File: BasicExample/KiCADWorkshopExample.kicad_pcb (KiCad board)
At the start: 2 copper layers, 100 x 100 mm, 21 parts, among them P1 USB_C_Plug_USB2.0, SW1 SW_Push, SW2 SW_Push, SW3 SW_Push, SW4 SW_Push, U1 BD30FC0WFP

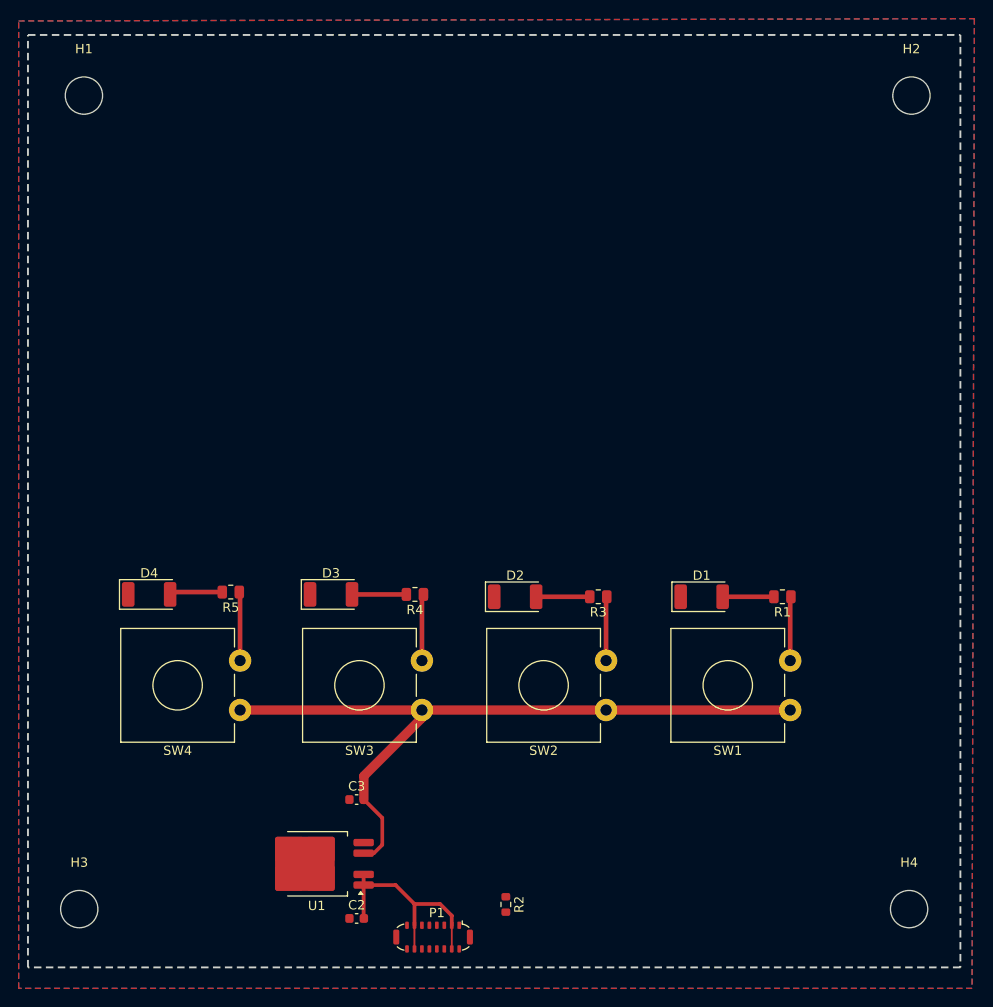
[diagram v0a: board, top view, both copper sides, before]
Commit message: complete simple tut
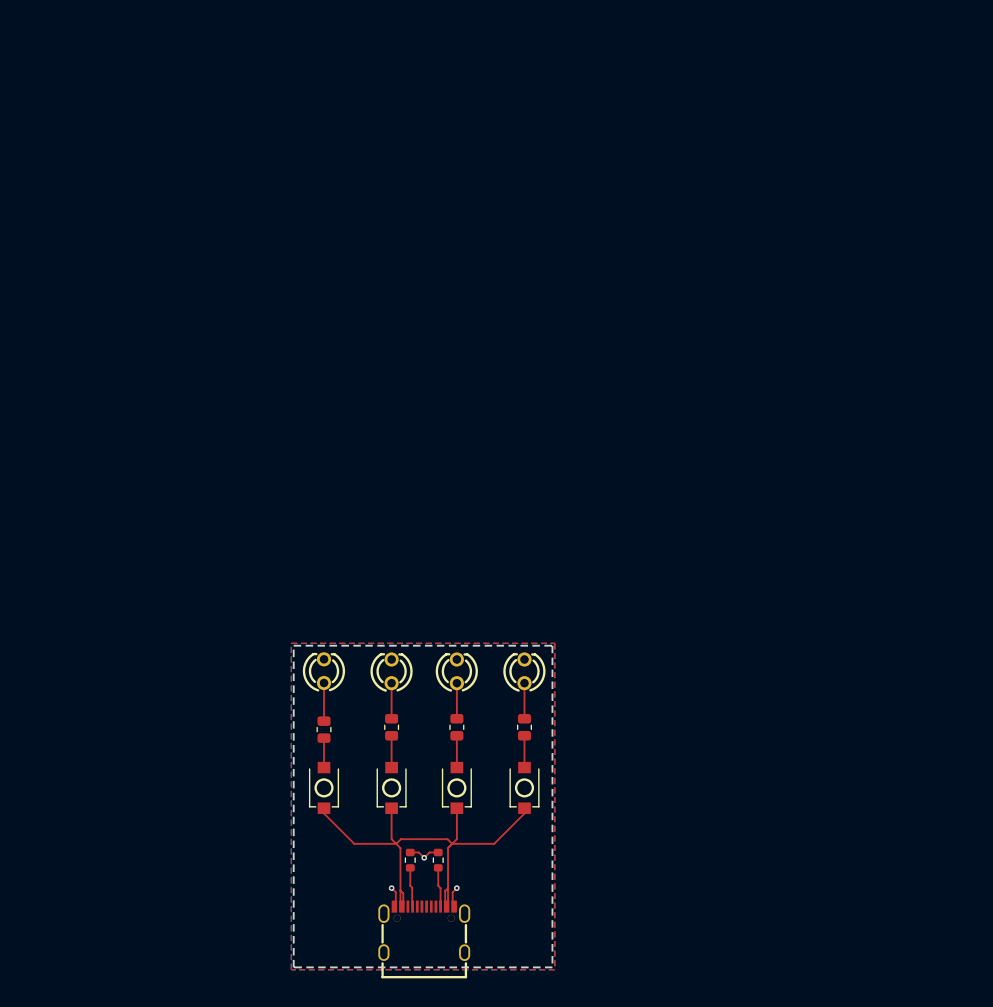
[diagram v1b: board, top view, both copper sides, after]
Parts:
- removed C2, C3: 10uF, Capacitor_SMD:C_0603_1608Metric
- removed D1, D2, D3, D4: LED, LED_SMD:LED_2010_5025Metric
- removed H1, H2, H3, H4: MountingHole, MountingHole:MountingHole_4mm
- removed P1: USB_C_Plug_USB2.0, Connector_USB:USB_C_Plug_ShenzhenJingTuoJin_918-118A2021Y40002_Vertical
- removed U1: BD30FC0WFP, Package_TO_SOT_SMD:TO-252-4
- added LED1: 204-10SURD/S530-A3-L, red:LED-TH_BD3.0-P2.54-FD, F.Cu at (103.2, 118.2)
- added LED2: 204-10SURD/S530-A3-L, red:LED-TH_BD3.0-P2.54-FD, F.Cu at (96.0, 118.2)
- added LED3: 204-10SURD/S530-A3-L, red:LED-TH_BD3.0-P2.54-FD, F.Cu at (89.0, 118.2)
- added LED4: 204-10SURD/S530-A3-L, red:LED-TH_BD3.0-P2.54-FD, F.Cu at (81.8, 118.2)
- added R6: 5K1, Resistor_SMD:R_0603_1608Metric, F.Cu at (94.0, 138.5)
- added USBC1: TYPE-C-31-M-12, usbc:USB-C_SMD-TYPE-C-31-M-12, F.Cu at (92.5, 145.9)
- R1, R3, R4, R5: value 520 -> 250
- SW1, SW2, SW3, SW4: value SW_Push -> TS-1088-AR02016; footprint Button_Switch_THT:SW_CW_GPTS203211B -> ts-1088:SW-SMD_L3.9-W3.0-P4.45
- moved R1 31.0 mm to (103.2, 124.2), turned to 90 degrees
- moved SW1 29.7 mm to (103.2, 130.8), turned to 90 degrees
- moved R3 20.6 mm to (96.0, 124.2), turned to 90 degrees
- moved SW2 18.0 mm to (96.0, 130.8), turned to 90 degrees
- moved R5 17.8 mm to (81.8, 124.5), turned to 90 degrees
- moved R4 14.5 mm to (89.0, 124.2), turned to 90 degrees
- moved SW4 12.3 mm to (81.8, 130.8), turned to 90 degrees
- moved R2 11.3 mm to (91.0, 138.5), turned to 90 degrees
- moved SW3 8.96 mm to (89.0, 130.8), turned to 90 degrees
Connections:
- SW1 pad 1: +3V3 -> VBUS
- SW2 pad 1: +3V3 -> VBUS
- SW3 pad 1: +3V3 -> VBUS
- SW4 pad 1: +3V3 -> VBUS
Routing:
- net +3V3: track 79.6 -> 0.00 mm
- net VBUS: track 23.9 -> 52.2 mm
- net GND: track 0.00 -> 7.80 mm, vias 0 -> 3
- net Net-(USBC1-CC1): track 0.00 -> 4.27 mm
- net Net-(USBC1-CC2): track 0.00 -> 4.26 mm
- net Net-(R5-Pad1): track 7.39 -> 3.16 mm
- net Net-(R4-Pad1): track 7.17 -> 3.41 mm
- net Net-(R3-Pad1): track 6.88 -> 3.41 mm
- net Net-(R1-Pad1): track 6.88 -> 3.41 mm
- net Net-(LED3-A): track 5.84 -> 3.82 mm
- net Net-(LED2-A): track 5.75 -> 3.82 mm
- net Net-(LED1-A): track 5.50 -> 3.82 mm
- net Net-(LED4-A): track 5.69 -> 4.09 mm
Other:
- board size 100 x 100 mm -> 27.8 x 34.5 mm

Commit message: traces
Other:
- board text added: "JAS"
- board text added: "JAS KiCAD Wrkshp 2024"
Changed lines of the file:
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@@
 		(layer "Edge.Cuts")
+	)
+	(gr_text "JAS KiCAD Wrkshp 2024"
+		(at 101.25 140.5 0)
+		(layer "B.SilkS")
+		(effects
+			(font
+				(size 1 1)
+				(thickness 0.2)
+				(bold yes)
+			)
+			(justify left bottom mirror)
+		)
+	)
+	(gr_text "JAS"
+		(at 101.75 149.25 0)
+		(layer "F.SilkS")
+		(effects
+			(font
+				(face "Lato")
+				(size 1.5 1.5)
+				(thickness 0.3)
+				(bold yes)
+			)
+			(justify left bottom)
+		)
+		(render_cache "JAS" 0
+			(polygon
+				(pts
+					(xy 102.525593 148.461573) (xy 102.52248 148.538488) (xy 102.511866 148.617227) (xy 102.493719 148.689818)
+					(xy 102.465709 148.761379) (xy 102.425482 148.829253) (xy 102.399563 148.861643) (xy 102.344183 148.913354)
+					(xy 102.279248 148.954181) (xy 102.246057 148.969354) (xy 102.174255 148.992126) (xy 102.095138 149.004388)
+					(xy 102.038328 149.006723) (xy 101.964718 149.003043) (xy 101.886951 148.992004) (xy 101.812648 148.975582)
+					(xy 101.81851 148.907072) (xy 101.824738 148.849187) (xy 101.841957 148.814382) (xy 101.88299 148.80046)
+					(xy 101.93538 148.809986) (xy 102.008797 148.819064) (xy 102.018178 148.819145) (xy 102.092804 148.81217)
+					(xy 102.137613 148.799361) (xy 102.201353 148.761438) (xy 102.225174 148.737445) (xy 102.264717 148.671734)
+					(xy 102.279762 148.629002) (xy 102.29405 148.55582) (xy 102.298739 148.481118) (xy 102.298813 148.469633)
+					(xy 102.298813 147.470924) (xy 102.525593 147.470924)
+				)
+			)
+			(polygon
+				(pts
+					(xy 104.080076 148.995) (xy 103.904588 148.995) (xy 103.853297 148.978879) (xy 103.823988 148.938579)
+					(xy 103.685502 148.578077) (xy 103.023115 148.578077) (xy 102.88463 148.938213) (xy 102.855321 148.97778)
+					(xy 102.80403 148.995) (xy 102.628541 148.995) (xy 102.864564 148.408817) (xy 103.089061 148.408817)
+					(xy 103.61919 148.408817) (xy 103.388014 147.823367) (xy 103.361819 147.752542) (xy 103.353576 147.724815)
+					(xy 103.342219 147.761451) (xy 103.320237 147.824466) (xy 103.089061 148.408817) (xy 102.864564 148.408817)
+					(xy 103.242201 147.470924) (xy 103.46605 147.470924)
+				)
+			)
+			(polygon
+				(pts
+					(xy 105.030792 147.723349) (xy 105.006978 147.750826) (xy 104.972906 147.760352) (xy 104.926011 147.741667)
+					(xy 104.865561 147.7021) (xy 104.798381 147.670584) (xy 104.780198 147.663998) (xy 104.705974 147.648814)
+					(xy 104.659665 147.646779) (xy 104.586038 147.652979) (xy 104.542062 147.664364) (xy 104.47591 147.697543)
+					(xy 104.458164 147.711625) (xy 104.412163 147.771331) (xy 104.407606 147.781235) (xy 104.391165 147.853318)
+					(xy 104.390753 147.867697) (xy 104.405894 147.941551) (xy 104.420062 147.964783) (xy 104.47536 148.016921)
+					(xy 104.498831 148.031828) (xy 104.566522 148.064686) (xy 104.61277 148.081653) (xy 104.682314 148.104748)
+					(xy 104.745394 148.125983) (xy 104.817359 148.151979) (xy 104.879483 148.178007) (xy 104.945828 148.213412)
+					(xy 104.998185 148.252379) (xy 105.048734 148.306152) (xy 105.083548 148.363387) (xy 105.107728 148.43666)
+					(xy 105.115662 148.512795) (xy 105.115788 148.524588) (xy 105.110894 148.598175) (xy 105.094545 148.674058)
+					(xy 105.080983 148.713265) (xy 105.047444 148.781018) (xy 105.003384 148.841394) (xy 104.979501 148.866772)
+					(xy 104.920604 148.915162) (xy 104.851669 148.954362) (xy 104.816468 148.969354) (xy 104.740322 148.992126)
+					(xy 104.664185 149.003767) (xy 104.597383 149.006723) (xy 104.515566 149.002579) (xy 104.437864 148.990147)
+					(xy 104.364277 148.969426) (xy 104.325174 148.954333) (xy 104.258456 148.921415) (xy 104.196374 148.8816)
+					(xy 104.138929 148.834887) (xy 104.109019 148.805956) (xy 104.172766 148.700809) (xy 104.197679 148.678094)
+					(xy 104.230286 148.668569) (xy 104.286339 148.693115) (xy 104.345381 148.736885) (xy 104.358147 148.745505)
+					(xy 104.424044 148.781539) (xy 104.459263 148.79643) (xy 104.533967 148.814797) (xy 104.603611 148.819145)
+					(xy 104.678353 148.813117) (xy 104.729274 148.800094) (xy 104.796698 148.766626) (xy 104.821964 148.746605)
+					(xy 104.868675 148.687528) (xy 104.879849 148.664539) (xy 104.898032 148.59351) (xy 104.9 148.557561)
+					(xy 104.887377 148.483509) (xy 104.87069 148.45278) (xy 104.818338 148.400757) (xy 104.792288 148.383904)
+					(xy 104.725227 148.351618) (xy 104.679082 148.335544) (xy 104.605563 148.312527) (xy 104.546458 148.294145)
+					(xy 104.474676 148.269214) (xy 104.412369 148.243953) (xy 104.346127 148.208341) (xy 104.294033 148.168848)
+					(xy 104.244341 148.113184) (xy 104.209769 148.053077) (xy 104.186628 147.980815) (xy 104.178033 147.906858)
+					(xy 104.177529 147.881985) (xy 104.184533 147.806599) (xy 104.205543 147.733629) (xy 104.209403 147.724082)
+					(xy 104.245826 147.656424) (xy 104.294647 147.596334) (xy 104.302093 147.588893) (xy 104.360707 147.54184)
+					(xy 104.424804 147.50631) (xy 104.451936 147.494738) (xy 104.522587 147.473082) (xy 104.600451 147.461422)
+					(xy 104.656367 147.4592) (xy 104.734749 147.463064) (xy 104.808695 147.474656) (xy 104.884911 147.496333)
+					(xy 104.891573 147.498768) (xy 104.962488 147.530862) (xy 105.028641 147.57274) (xy 105.084647 147.619302)
+				)
+			)
+		)
 	)
 	(segment

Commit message: new switch & board in production
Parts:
- removed the R5 at (81.8, 124.5)
- added G***: LOGO, Graphics:jas_logo_sm, F.Cu at (99.9, 141.5)
- added H1: MountingHole_Pad, MountingHole:MountingHole_4.3mm_M4_DIN965_Pad, F.Cu at (111.6, 142.6)
- added R2: 120, Resistor_SMD:R_0805_2012Metric, F.Cu at (98.5, 124.8)
- R1, R3, R4: value 250 -> 120
- SW1, SW2, SW3, SW4: value TS-1088-AR02016 -> TS-1187A-B-A-B; footprint ts-1088:SW-SMD_L3.9-W3.0-P4.45 -> ts1088:SW-SMD_4P-L5.1-W5.1-P3.70-LS6.5-TL-2
- moved SW4 29.6 mm to (111.3, 129.2), turned to 180 degrees
- moved SW1 20.0 mm to (83.3, 129.2), turned to 180 degrees
- moved SW3 12.9 mm to (101.8, 129.2), turned to 180 degrees
- moved LED1 9.43 mm to (111.4, 123.0)
- moved R4 9.02 mm to (80.0, 124.8)
- moved LED2 7.51 mm to (101.9, 122.9)
- moved R3 6.72 mm to (89.3, 124.8)
- moved LED3 6.02 mm to (92.7, 123.0)
- moved USBC1 5.97 mm to (87.4, 142.8)
- moved R5 5.58 mm to (88.6, 137.1)
- moved LED4 5.05 mm to (83.4, 123.0)
- moved R6 5.00 mm to (86.2, 137.1)
- moved R1 4.78 mm to (108.0, 124.8)
- moved SW2 3.74 mm to (92.6, 129.2), turned to 180 degrees
- renumbered R6 to R5, R2 to R6
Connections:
- R1 pad 1: Net-(R1-Pad1) -> Net-(SW4-D)
- R3 pad 1: Net-(R3-Pad1) -> Net-(SW2-D)
- R3 pad 2: Net-(LED2-A) -> Net-(LED3-A)
- R4 pad 1: Net-(R4-Pad1) -> Net-(SW1-D)
- R4 pad 2: Net-(LED3-A) -> Net-(LED4-A)
- SW1 pad 1: VBUS -> unconnected-(SW1-A-Pad1)
- SW1 pad 2: Net-(R1-Pad1) -> VBUS
- SW2 pad 1: VBUS -> unconnected-(SW2-A-Pad1)
- SW2 pad 2: Net-(R3-Pad1) -> VBUS
- SW3 pad 1: VBUS -> unconnected-(SW3-A-Pad1)
- SW3 pad 2: Net-(R4-Pad1) -> VBUS
- SW4 pad 1: VBUS -> unconnected-(SW4-A-Pad1)
- SW4 pad 2: Net-(R5-Pad1) -> VBUS
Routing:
- net VBUS: track 52.2 -> 46.2 mm
- net GND: track 7.80 -> 2.09 mm, vias 3 -> 0
- net Net-(R4-Pad1): track 3.41 -> 0.00 mm
- net Net-(R3-Pad1): track 3.41 -> 0.00 mm
- net Net-(R1-Pad1): track 3.41 -> 0.00 mm
- net Net-(R5-Pad1): track 3.16 -> 0.00 mm
- net Net-(USBC1-CC1): track 4.27 -> 2.47 mm
- net Net-(SW4-D): track 0.00 -> 1.74 mm
- net Net-(SW3-D): track 0.00 -> 1.74 mm
- net Net-(SW2-D): track 0.00 -> 1.74 mm
- net Net-(SW1-D): track 0.00 -> 1.74 mm
- net Net-(USBC1-CC2): track 4.26 -> 2.68 mm
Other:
- board size 27.8 x 34.5 mm -> 37.3 x 26.8 mm
- board text added: "JAS KiCAD Workshop Fall 2024"
- board text added: "JLCJLCJLCJLC"
- board text removed: "JAS"
- board text removed: "JAS KiCAD Wrkshp 2024"
